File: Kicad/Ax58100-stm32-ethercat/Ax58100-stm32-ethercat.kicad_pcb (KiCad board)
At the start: 4 copper layers, 94.5 x 59.2 mm, 131 parts, among them J1 Conn_01x06_Pin, J10 Conn_01x02_Pin, J11 Stepper 2, J12 Serial usart1, J13 Stepper 1, J14 I2C bus2, J2 Encoder 1, J3 Conn_01x06_Pin, J4 Encoder 2, J5 Conn_01x06_Pin, J6 Encoder 4, J7 DAC1, J8 Encoder 3, J9 STLINK, SW1 SW PB, U1 AMS1117-1.2, U2 AX58100, U3 24LC32A, U4 STM32F407VGT6, U5 AMS1117-3.3, Y1 NXK25.000AE12F-KAB6-12, Y2 8 MHz

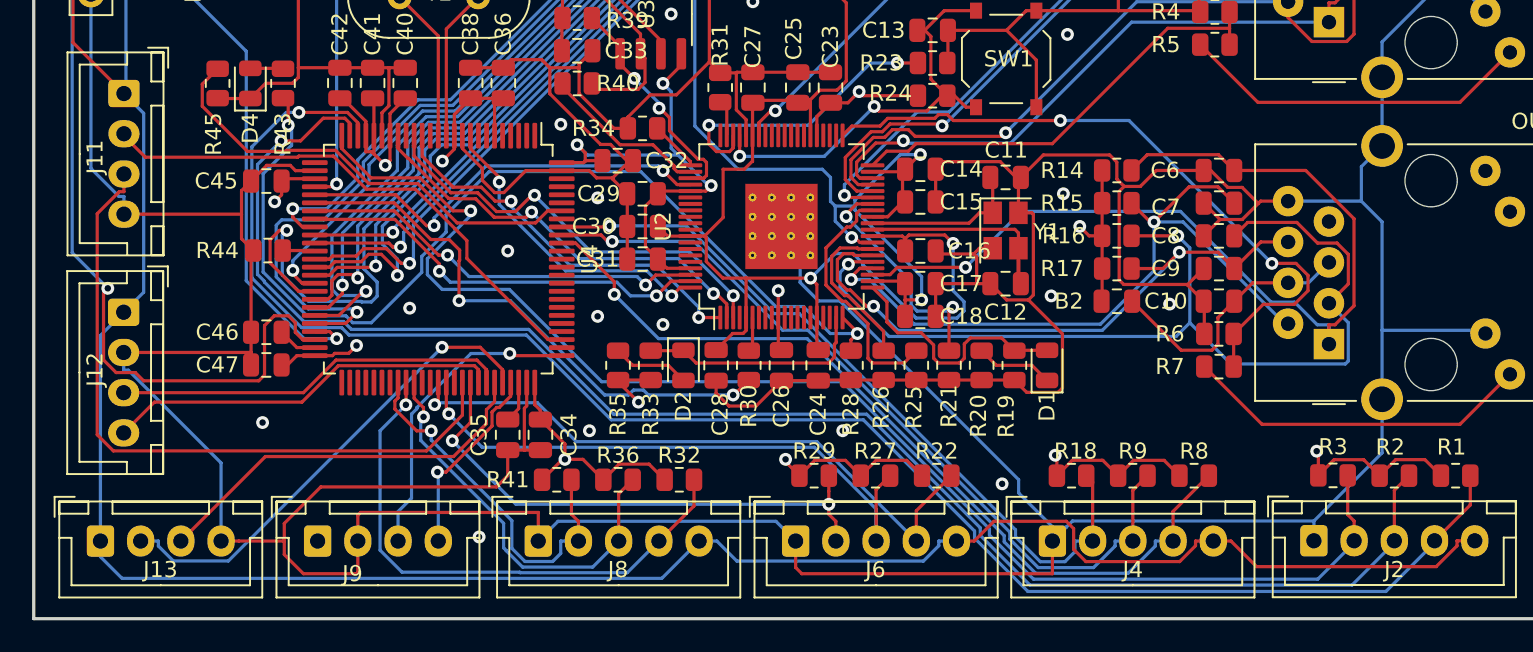
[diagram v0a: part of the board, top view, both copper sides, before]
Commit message: Added optional pull-down to step generators
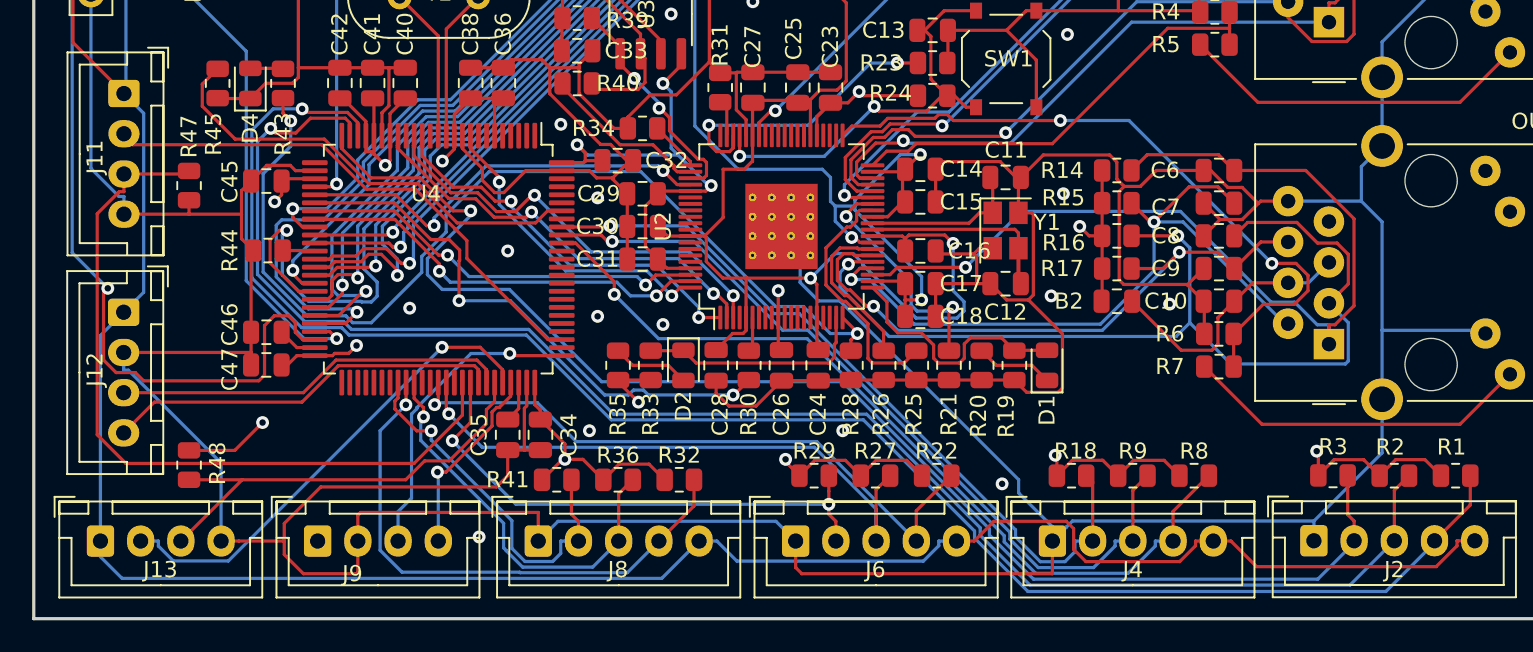
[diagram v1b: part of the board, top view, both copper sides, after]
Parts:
- added R47: NC, Resistor_SMD:R_0805_2012Metric, F.Cu at (148.6, 96.0)
- added R48: NC, Resistor_SMD:R_0805_2012Metric, F.Cu at (148.6, 113.4)
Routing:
- net GND: track 676.2 -> 682.4 mm
- net STEP2_STEP: track 43.1 -> 47.9 mm
- net STEP1_STEP: track 24.8 -> 28.1 mm
- net ENC1_B: track 99.3 -> 100.3 mm
- net ENC1_A: track 104.9 -> 105.7 mm

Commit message: First component placement
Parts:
- removed J14: I2C bus2, Connector_PinHeader_2.54mm:PinHeader_1x04_P2.54mm_Vertical
- removed J8: Encoder 3, Connector_JST:JST_XH_B5B-XH-A_1x05_P2.50mm_Vertical
- removed R22, R27, R3, R32, R36, R41, R8: 1k, Resistor_SMD:R_0805_2012Metric
- added D10: Yellow led, LED_SMD:LED_0603_1608Metric, F.Cu at (100.6, 34.3)
- added D11: Red led, LED_SMD:LED_0603_1608Metric, F.Cu at (100.5, 62.2)
- added D12: Yellow led, LED_SMD:LED_0603_1608Metric, F.Cu at (100.6, 29.1)
- added D13: Red led, LED_SMD:LED_0603_1608Metric, F.Cu at (100.5, 67.5)
- added D14: Red led, LED_SMD:LED_0603_1608Metric, F.Cu at (100.5, 30.8)
- added D15: Red led, LED_SMD:LED_0603_1608Metric, F.Cu at (100.5, 36.1)
- added D16: Red led, LED_SMD:LED_0603_1608Metric, F.Cu at (100.5, 41.3)
- added D17: Red led, LED_SMD:LED_0603_1608Metric, F.Cu at (100.5, 46.5)
- added D23: Yellow led, LED_SMD:LED_0603_1608Metric, F.Cu at (100.5, 50.0)
- added D25: Yellow led, LED_SMD:LED_0603_1608Metric, F.Cu at (100.6, 55.2)
- added D27: Yellow led, LED_SMD:LED_0603_1608Metric, F.Cu at (100.6, 60.5)
- added D29: Yellow led, LED_SMD:LED_0603_1608Metric, F.Cu at (100.6, 65.7)
- added D6: Yellow led, LED_SMD:LED_0603_1608Metric, F.Cu at (100.6, 44.8)
- added D7: Red led, LED_SMD:LED_0603_1608Metric, F.Cu at (100.6, 51.8)
- added D8: Yellow led, LED_SMD:LED_0603_1608Metric, F.Cu at (100.6, 39.5)
- added D9: Red led, LED_SMD:LED_0603_1608Metric, F.Cu at (100.5, 57.0)
- added J15: In1-4, TerminalBlock:TerminalBlock_bornier-4_P5.08mm, F.Cu at (107.0, 44.5)
- added J16: 24V Field, TerminalBlock:TerminalBlock_bornier-2_P5.08mm, F.Cu at (82.7, 45.2)
- added J17: In5-8, TerminalBlock:TerminalBlock_bornier-4_P5.08mm, F.Cu at (107.0, 66.0)
- added J19: Step3, TerminalBlock:TerminalBlock_bornier-3_P5.08mm, F.Cu at (122.9, 71.6)
- added J20: Step4, TerminalBlock:TerminalBlock_bornier-3_P5.08mm, F.Cu at (122.9, 87.4)
- added J21: THCAD, TerminalBlock:TerminalBlock_bornier-4_P5.08mm, F.Cu at (122.9, 108.5)
- added R49: 1k, Resistor_SMD:R_0603_1608Metric, F.Cu at (100.5, 43.0)
- added R50: 1k, Resistor_SMD:R_0603_1608Metric, F.Cu at (100.5, 37.8)
- added R51: 1k, Resistor_SMD:R_0603_1608Metric, F.Cu at (100.5, 32.6)
- added R52: 1k, Resistor_SMD:R_0603_1608Metric, F.Cu at (100.5, 27.3)
- added R53: 4.7k, Resistor_SMD:R_0805_2012Metric, F.Cu at (116.8, 50.5)
- added R57: 1k, Resistor_SMD:R_0603_1608Metric, F.Cu at (100.5, 48.3)
- added R58: 1k, Resistor_SMD:R_0603_1608Metric, F.Cu at (100.5, 53.5)
- added R59: 1k, Resistor_SMD:R_0603_1608Metric, F.Cu at (100.5, 58.7)
- added R60: 1k, Resistor_SMD:R_0603_1608Metric, F.Cu at (100.5, 64.0)
- added RN1: 40k, Resistor_SMD:R_Array_Convex_4x0603, F.Cu at (90.0, 39.5)
- added RN2: 40k, Resistor_SMD:R_Array_Convex_4x0603, F.Cu at (89.7, 57.8)
- added RN3: 1k, Resistor_SMD:R_Array_Convex_4x0603, F.Cu at (95.3, 57.8)
- added RN4: 1k, Resistor_SMD:R_Array_Convex_4x0603, F.Cu at (95.9, 39.5)
- added RN5: 330, Resistor_SMD:R_Array_Convex_4x0603, F.Cu at (95.1, 94.2)
- added U10: TXB0104PW, Package_SO:TSSOP-14_4.4x5mm_P0.65mm, F.Cu at (116.1, 74.6)
- added U11: MAX3485CSA/ESA, Package_SO:SO-8_3.9x4.9mm_P1.27mm, F.Cu at (115.6, 92.9)
- added U6: TLP292-4, Package_SO:SOIC-16_4.55x10.3mm_P1.27mm, F.Cu at (92.7, 32.0)
- added U7: TLP291-4, Package_SO:SOIC-16_4.55x10.3mm_P1.27mm, F.Cu at (97.1, 82.8)
- added U8: TLP292-4, Package_SO:SOIC-16_4.55x10.3mm_P1.27mm, F.Cu at (92.8, 50.4)
- added U9: TXB0104PW, Package_SO:TSSOP-14_4.4x5mm_P0.65mm, F.Cu at (115.8, 42.7)
- J1: value Conn_01x06_Pin -> Out_opt
- J10: value Conn_01x02_Pin -> 5V Power IN; footprint Connector_JST:JST_XH_B2B-XH-A_1x02_P2.50mm_Vertical -> TerminalBlock:TerminalBlock_bornier-2_P5.08mm
- J11: value Stepper 2 -> Step1; footprint Connector_JST:JST_XH_B4B-XH-A_1x04_P2.50mm_Vertical -> TerminalBlock:TerminalBlock_bornier-3_P5.08mm
- J13: value Stepper 1 -> Step2; footprint Connector_JST:JST_XH_B4B-XH-A_1x04_P2.50mm_Vertical -> TerminalBlock:TerminalBlock_bornier-3_P5.08mm
- J2: value Encoder 1 -> Output1-2; footprint Connector_JST:JST_XH_B5B-XH-A_1x05_P2.50mm_Vertical -> TerminalBlock:TerminalBlock_bornier-4_P5.08mm
- J3: value Conn_01x06_Pin -> In_opt1
- J4: value Encoder 2 -> Output3-4; footprint Connector_JST:JST_XH_B5B-XH-A_1x05_P2.50mm_Vertical -> TerminalBlock:TerminalBlock_bornier-4_P5.08mm
- J5: value Conn_01x06_Pin -> In_opt2
- J6: value Encoder 4 -> DAC; footprint Connector_JST:JST_XH_B5B-XH-A_1x05_P2.50mm_Vertical -> TerminalBlock:TerminalBlock_bornier-3_P5.08mm
- J7: value DAC1 -> Encoder; footprint Connector_JST:JST_XH_B3B-XH-A_1x03_P2.50mm_Vertical -> TerminalBlock:TerminalBlock_bornier-5_P5.08mm
- R18, R2: value 1k -> 4.7k
- R47: value NC -> 120
- R48: value NC -> 4.7k
- moved J1 195.8 mm to (38.1, 103.5), turned to 90 degrees
- moved OUT1 187.9 mm to (47.4, 30.2), turned to 90 degrees
- moved R7 176.7 mm to (54.3, 28.8), turned to 0 degrees
- moved IN1 175.7 mm to (47.4, 50.2), turned to 90 degrees
- moved R6 175.0 mm to (54.3, 30.8), turned to 0 degrees
- moved C10 173.3 mm to (54.3, 32.9), turned to 180 degrees
- moved C9 171.7 mm to (54.3, 34.9), turned to 180 degrees
- moved C8 170.1 mm to (54.3, 36.9), turned to 180 degrees
- moved D1 169.5 mm to (37.0, 67.9), turned to -90 degrees
- moved C7 168.7 mm to (54.3, 39.0), turned to 180 degrees
- moved C6 167.3 mm to (54.3, 41.0), turned to 180 degrees
- moved J3 166.2 mm to (51.4, 110.5)
- moved R19 165.6 mm to (39.0, 67.9), turned to -90 degrees
- moved R5 162.5 mm to (54.5, 48.8), turned to 0 degrees
- moved C12 162.4 mm to (39.6, 73.0), turned to 0 degrees
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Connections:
- J11 pad 1: +5V -> STEP1_DIR_OUT
- J11 pad 2: STEP2_DIR -> STEP1_STEP_OUT
- J11 pad 3: STEP2_STEP -> GND
- J13 pad 1: +5V -> STEP2_DIR_OUT
- J13 pad 2: STEP1_DIR -> STEP2_STEP_OUT
- J13 pad 3: STEP1_STEP -> GND
- J2 pad 1: GND -> Net-(J2-Pin_1)
- J2 pad 2: ENC1_Z -> Net-(J2-Pin_2)
- J2 pad 3: ENC1_B -> Net-(J2-Pin_3)
- J2 pad 4: ENC1_A -> Net-(J2-Pin_4)
- J4 pad 1: GND -> Net-(J4-Pin_1)
- J4 pad 2: ENC2_Z -> Net-(J4-Pin_2)
- J4 pad 3: ENC2_B -> Net-(J4-Pin_3)
- J4 pad 4: ENC2_A -> Net-(J4-Pin_4)
- J6 pad 1: GND -> +3.3V
- J6 pad 2: ENC4_Z -> DAC1
- J6 pad 3: ENC4_B -> GND
- J7 pad 1: +3.3V -> +5V
- J7 pad 2: DAC1 -> ENC_A
- J7 pad 3: GND -> ENC_B
- R1 pad 1: ENC1_A -> ENC_A
- R1 pad 2: +3.3V -> +5V
- R18 pad 1: ENC2_Z -> GND
- R18 pad 2: +3.3V -> STEP4_STEP
- R2 pad 1: ENC1_B -> GND
- R2 pad 2: +3.3V -> STEP3_STEP
- R29 pad 1: ENC4_Z -> ENC_Z
- R29 pad 2: +3.3V -> +5V
- R47 pad 1: STEP2_STEP -> Net-(J21-Pin_2)
- R47 pad 2: GND -> Net-(J21-Pin_3)
- R48 pad 1: STEP1_STEP -> GND
- R48 pad 2: GND -> STEP1_STEP
- R9 pad 1: ENC2_B -> ENC_B
- R9 pad 2: +3.3V -> +5V
- U4 pad 23: ENC1_A -> ENC_A
- U4 pad 24: ENC1_B -> ENC_B
- U4 pad 25: ENC1_Z -> THCAD_CTR
- U4 pad 26: unconnected-(U4-PA3-Pad26) -> ENC_Z
- U4 pad 3: unconnected-(U4-PE4-Pad3) -> STEP4_DIR
- U4 pad 4: unconnected-(U4-PE5-Pad4) -> STEP4_STEP
- U4 pad 47: I2C2_SCL -> unconnected-(U4-PB10-Pad47)
- U4 pad 48: I2C2_SDA -> unconnected-(U4-PB11-Pad48)
- U4 pad 58: ENC3_Z -> STEP3_DIR
- U4 pad 59: ENC3_A -> STEP3_STEP
- U4 pad 60: ENC3_B -> unconnected-(U4-PD13-Pad60)
- U4 pad 63: ENC4_A -> unconnected-(U4-PC6-Pad63)
- U4 pad 64: ENC4_B -> unconnected-(U4-PC7-Pad64)
- U4 pad 65: unconnected-(U4-PC8-Pad65) -> STEP2_DIR
- U4 pad 67: ENC4_Z -> unconnected-(U4-PA8-Pad67)
- U4 pad 78: STEP2_DIR -> unconnected-(U4-PC10-Pad78)
- U4 pad 90: ENC2_A -> unconnected-(U4-PB4-Pad90)
- U4 pad 91: ENC2_B -> unconnected-(U4-PB5-Pad91)
- U4 pad 92: ENC2_Z -> unconnected-(U4-PB6-Pad92)
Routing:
- net GND: track 682.4 -> 0.00 mm, vias 24 -> 0
- net +5V: track 289.8 -> 0.00 mm, vias 1 -> 0
- net +3.3V: track 209.3 -> 0.00 mm, vias 23 -> 0
- net +3.3VA: track 109.3 -> 0.00 mm, vias 4 -> 0
- net ENC1_A: track 105.7 -> 0.00 mm, vias 1 -> 0
- net ENC1_B: track 100.3 -> 0.00 mm, vias 1 -> 0
- net +1V2: track 97.9 -> 0.00 mm, vias 2 -> 0
- net IO1: track 93.0 -> 0.00 mm, vias 1 -> 0
- net ENC1_Z: track 86.5 -> 0.00 mm, vias 1 -> 0
- net IO2: track 83.8 -> 0.00 mm, vias 1 -> 0
- net IO3: track 81.9 -> 0.00 mm, vias 1 -> 0
- net IO4: track 80.7 -> 0.00 mm, vias 1 -> 0
- net IO8: track 77.5 -> 0.00 mm, vias 1 -> 0
- net P0_TXON: track 75.4 -> 0.00 mm, vias 1 -> 0
- net IO5: track 72.0 -> 0.00 mm, vias 1 -> 0
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- removed copper zone on In2.Cu, net +3.3V
- removed copper zone on B.Cu, net GND
- removed copper zone on F.Cu, net GND
- removed copper zone on In1.Cu, net GND
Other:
- board size 94.5 x 59.2 mm -> 95.3 x 89.4 mm

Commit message: Two-layer now
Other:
- copper layers 4 -> 2
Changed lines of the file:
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@@
   (layers
     (0 "F.Cu" signal)
-    (1 "In1.Cu" power "GND.Cu")
-    (2 "In2.Cu" power "Power.Cu")
     (31 "B.Cu" signal)
     (32 "B.Adhes" user "B.Adhesive")
@@
       (layer "F.Mask" (type "Top Solder Mask") (thickness 0.01))
       (layer "F.Cu" (type "copper") (thickness 0.035))
-      (layer "dielectric 1" (type "prepreg") (thickness 0.1) (material "FR4") (epsilon_r 4.5) (loss_tangent 0.02))
-      (layer "In1.Cu" (type "copper") (thickness 0.035))
-      (layer "dielectric 2" (type "core") (thickness 1.24) (material "FR4") (epsilon_r 4.5) (loss_tangent 0.02))
-      (layer "In2.Cu" (type "copper") (thickness 0.035))
-      (layer "dielectric 3" (type "prepreg") (thickness 0.1) (material "FR4") (epsilon_r 4.5) (loss_tangent 0.02))
+      (layer "dielectric 1" (type "core") (thickness 1.51) (material "FR4") (epsilon_r 4.5) (loss_tangent 0.02))
       (layer "B.Cu" (type "copper") (thickness 0.035))
       (layer "B.Mask" (type "Bottom Solder Mask") (thickness 0.01))

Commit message: wip
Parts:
- removed the U10 at (116.1, 74.6)
- removed the U9 at (115.8, 42.7)
- added C50: 0.1uF, Capacitor_SMD:C_0805_2012Metric, F.Cu at (167.5, 75.9)
- added C51: 0.1uF, Capacitor_SMD:C_0805_2012Metric, F.Cu at (167.5, 78.0)
- added C52: 0.1uF, Capacitor_SMD:C_0805_2012Metric, F.Cu at (169.2, 112.3)
- added U12: TXS0108EPW, Package_SO:TSSOP-20_4.4x6.5mm_P0.65mm, F.Cu at (167.4, 82.5)
- U4: renamed from U7; value TLP291-4 -> TLP292-4
- moved R14 88.8 mm to (141.6, 123.7), turned to -90 degrees
- moved C2 85.3 mm to (139.5, 123.7), turned to -90 degrees
- moved C4 82.1 mm to (137.4, 123.7), turned to 90 degrees
- moved C1 72.2 mm to (141.0, 102.1), turned to 90 degrees
- moved SW1 64.4 mm to (97.3, 109.4)
- moved C3 64.4 mm to (137.2, 101.8), turned to 90 degrees
- moved U7 62.9 mm to (133.1, 112.7), turned to -90 degrees
- moved RN1 61.4 mm to (149.5, 122.7)
- moved C5 61.3 mm to (135.2, 92.1), turned to 0 degrees
- moved U4 61.2 mm to (149.4, 114.8)
- moved C6 60.3 mm to (135.1, 101.8), turned to 90 degrees
- moved C42 60.3 mm to (96.9, 117.8)
- moved R47 60.3 mm to (96.9, 115.8)
- moved R46 60.3 mm to (96.9, 113.8)
- moved R1 59.9 mm to (151.6, 96.8)
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- renumbered B7 to B1, B6 to B2, B5 to B3, B2 to B4, B1 to B5, B4 to B6, B3 to B7, C32 to C1, C42 to C10, C49 to C11, C48 to C12, C45 to C13, C46 to C14, C47 to C15, C44 to C16, C43 to C17, C33 to C18, C31 to C19, C34 to C2, C30 to C20, C29 to C21, C28 to C22, C27 to C23, C10 to C24, C9 to C25, C8 to C26, C7 to C27, C6 to C28, C5 to C29, C36 to C3, C4 to C30, C3 to C31, C2 to C32, C1 to C33, C26 to C34, C25 to C35, C24 to C36, C23 to C37, C22 to C38, C21 to C39, C35 to C4, C20 to C40, C19 to C41, C13 to C42, C18 to C43, C17 to C44, C16 to C45, C15 to C46, C14 to C47, C12 to C48, C11 to C49, C37 to C5, C38 to C6, C39 to C7, C40 to C8, C41 to C9, D12 to D1, D7 to D10, D25 to D11, D9 to D12, D27 to D13, D11 to D14, D29 to D15, D13 to D16, D5 to D17, D4 to D18, D3 to D19, D14 to D2, D2 to D20, D1 to D21, D10 to D3, D15 to D4, D8 to D5, D16 to D6, D6 to D7, D17 to D8, D23 to D9, J11 to J1, J16 to J11, J6 to J12, J7 to J13, J5 to J14, J9 to J15, J12 to J16, J3 to J17, J1 to J18, J13 to J2, J19 to J3, J20 to J4, J21 to J5, J15 to J6, J17 to J7, J2 to J8, J4 to J9, R48 to R1, R57 to R10, R58 to R11, R59 to R12, R60 to R13, R35 to R14, R29 to R15, R9 to R16, R1 to R17, R46 to R18, R45 to R19, R53 to R2, R43 to R20, R44 to R21, R42 to R22, R40 to R23, R39 to R24, R38 to R25, R37 to R26, R33 to R27, R34 to R28, R17 to R29, R2 to R3, R16 to R30, R15 to R31, R14 to R32, R13 to R33, R12 to R34, R11 to R35, R10 to R36, R31 to R37, R30 to R38, R7 to R39, R18 to R4, R6 to R40, R5 to R41, R4 to R42, R28 to R43, R26 to R44, R25 to R45, R24 to R46, R23 to R47, R21 to R48, R20 to R49, R47 to R5, R19 to R50, R52 to R6, R51 to R7, R50 to R8, R49 to R9, RN5 to RN1, RN4 to RN2, RN1 to RN4, RN2 to RN5, U1 to U10, U2 to U11, U11 to U3, U6 to U5, U8 to U6, U4 to U7, U5 to U8, U3 to U9, Y2 to Y1, Y1 to Y2
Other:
- board size 95.3 x 89.4 mm -> 95.3 x 87.9 mm

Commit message: resistor overhaul
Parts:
- removed RN1: 330, Resistor_SMD:R_Array_Convex_4x0603
- removed RN2, RN3: 1k, Resistor_SMD:R_Array_Convex_4x0603
- removed RN4, RN5: 40k, Resistor_SMD:R_Array_Convex_4x0603
- added R51: 1k, Resistor_SMD:R_0603_1608Metric, F.Cu at (147.6, 81.0)
- added R52: 1k, Resistor_SMD:R_0603_1608Metric, F.Cu at (147.6, 82.5)
- added R53: 1k, Resistor_SMD:R_0603_1608Metric, F.Cu at (147.6, 84.1)
- added R54: 1k, Resistor_SMD:R_0603_1608Metric, F.Cu at (147.6, 85.6)
- added R55: 1k, Resistor_SMD:R_0603_1608Metric, F.Cu at (147.3, 62.5)
- added R56: 1k, Resistor_SMD:R_0603_1608Metric, F.Cu at (147.3, 64.0)
- added R57: 1k, Resistor_SMD:R_0603_1608Metric, F.Cu at (147.3, 65.5)
- added R58: 1k, Resistor_SMD:R_0603_1608Metric, F.Cu at (147.3, 67.1)
- added R59: 330, Resistor_SMD:R_0603_1608Metric, F.Cu at (147.1, 107.4)
- added R60: 330, Resistor_SMD:R_0603_1608Metric, F.Cu at (148.6, 107.4)
- added R61: 330, Resistor_SMD:R_0603_1608Metric, F.Cu at (150.1, 107.4)
- added R62: 330, Resistor_SMD:R_0603_1608Metric, F.Cu at (151.6, 107.4)
- added R63: 39k, Resistor_SMD:R_0603_1608Metric, F.Cu at (143.0, 62.5)
- added R64: 39k, Resistor_SMD:R_0603_1608Metric, F.Cu at (143.0, 64.0)
- added R65: 39k, Resistor_SMD:R_0603_1608Metric, F.Cu at (143.0, 65.5)
- added R66: 39k, Resistor_SMD:R_0603_1608Metric, F.Cu at (143.0, 67.1)
- added R67: 39k, Resistor_SMD:R_0603_1608Metric, F.Cu at (142.7, 81.0)
- added R68: 39k, Resistor_SMD:R_0603_1608Metric, F.Cu at (142.7, 82.5)
- added R69: 39k, Resistor_SMD:R_0603_1608Metric, F.Cu at (142.7, 84.1)
- added R70: 39k, Resistor_SMD:R_0603_1608Metric, F.Cu at (142.7, 85.6)

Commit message: Might be in final shape.
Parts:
- J1, J2, J3, J4: footprint TerminalBlock:TerminalBlock_bornier-3_P5.08mm -> Connector_Phoenix_MC:PhoenixContact_MCV_1,5_3-G-3.5_1x03_P3.50mm_Vertical
- J10: renamed from J13; footprint TerminalBlock:TerminalBlock_bornier-5_P5.08mm -> Connector_Phoenix_MC:PhoenixContact_MCV_1,5_5-G-3.5_1x05_P3.50mm_Vertical
- J11: renamed from J10; footprint TerminalBlock:TerminalBlock_bornier-2_P5.08mm -> Connector_Phoenix_MC:PhoenixContact_MCV_1,5_2-G-3.5_1x02_P3.50mm_Vertical
- J12: renamed from J11; footprint TerminalBlock:TerminalBlock_bornier-2_P5.08mm -> Connector_Phoenix_MC:PhoenixContact_MCV_1,5_2-G-3.5_1x02_P3.50mm_Vertical
- J13: renamed from J12; footprint TerminalBlock:TerminalBlock_bornier-3_P5.08mm -> Connector_Phoenix_MC:PhoenixContact_MCV_1,5_3-G-3.5_1x03_P3.50mm_Vertical
- J5, J6, J7, J8, J9: footprint TerminalBlock:TerminalBlock_bornier-4_P5.08mm -> Connector_Phoenix_MC:PhoenixContact_MCV_1,5_4-G-3.5_1x04_P3.50mm_Vertical
- R10: renamed from R1; value 4.7k -> 4k7
- R13: renamed from R2; value 4.7k -> 4k7
- R17: renamed from R3; value 4.7k -> 4k7
- R2: renamed from R6; value 1k -> 4k7
- R28: renamed from R4; value 4.7k -> 4k7
- R3: renamed from R7; value 1k -> 4k7
- R4: renamed from R8; value 1k -> 4k7
- R5: renamed from R9; value 1k -> 4k7
- R6: renamed from R10; value 1k -> 4k7
- R7: renamed from R11; value 1k -> 4k7
- R8: renamed from R12; value 1k -> 4k7
- R9: renamed from R13; value 1k -> 4k7
- moved J14 51.3 mm to (125.5, 86.2), turned to 90 degrees
- moved J16 46.2 mm to (118.6, 86.2), turned to 90 degrees
- moved R56 44.0 mm to (112.0, 91.2), turned to 90 degrees
- moved C13 32.2 mm to (129.0, 55.1)
- moved C15 32.2 mm to (127.0, 55.1)
- moved J9 29.6 mm to (158.4, 103.5), turned to -90 degrees
- moved J5 26.3 mm to (174.9, 106.0), turned to -90 degrees
- moved R12 26.1 mm to (152.1, 112.9)
- moved J8 24.8 mm to (158.4, 87.0), turned to -90 degrees
- moved D18 22.7 mm to (125.7, 68.6)
- moved R38 22.7 mm to (129.8, 68.6)
- moved D17 22.7 mm to (127.8, 68.6)
- moved R39 22.7 mm to (123.7, 68.6)
- moved R15 22.7 mm to (150.1, 112.9)
- moved R62 21.1 mm to (104.6, 91.2), turned to 90 degrees
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- renumbered B4 to B2, B5 to B3, B2 to B4, B3 to B5, C52 to C1, C7 to C10, C8 to C11, C9 to C12, C12 to C13, C10 to C14, C17 to C15, C22 to C16, C13 to C17, C14 to C18, C15 to C19, C50 to C2, C34 to C20, C36 to C21, C18 to C22, C19 to C23, C20 to C24, C21 to C25, C11 to C26, C23 to C27, C24 to C28, C25 to C29, C51 to C3, C26 to C30, C27 to C31, C28 to C32, C29 to C33, C30 to C34, C31 to C35, C32 to C36, C33 to C37, C16 to C38, C35 to C39, C2 to C4, C37 to C40, C38 to C41, C39 to C42, C40 to C43, C41 to C44, C42 to C45, C43 to C46, C44 to C47, C45 to C48, C46 to C49, C4 to C5, C47 to C50, C48 to C51, C49 to C52, C1 to C6, C3 to C7, C5 to C8, C6 to C9, D19 to D18, D20 to D19, D18 to D20, J17 to J14, J16 to J15, J14 to J16, J15 to J17, R5 to R1, R62 to R11, R17 to R12, R61 to R14, R16 to R15, R60 to R16, R15 to R18, R55 to R19, R56 to R20, R57 to R21, R58 to R22, R51 to R23, R52 to R24, R53 to R25, R54 to R26, R59 to R27, R19 to R29, R63 to R30, R64 to R31, R65 to R32, R66 to R33, R67 to R34, R68 to R35, R69 to R36, R70 to R37, R18 to R38, R22 to R39, R21 to R40, R26 to R41, R38 to R42, R25 to R43, R24 to R44, R28 to R45, R23 to R46, R27 to R47, R29 to R48, R30 to R49, R31 to R50, R32 to R51, R33 to R52, R34 to R53, R35 to R54, R36 to R55, R14 to R56, R37 to R57, R39 to R58, R40 to R59, R41 to R60, R42 to R61, R20 to R62, R43 to R63, R44 to R64, R45 to R65, R46 to R66, R47 to R67, R48 to R68, R49 to R69, R50 to R70, U3 to U1, U11 to U10, U12 to U2, U4 to U3, U5 to U4, U6 to U5, U7 to U6, U8 to U7, U9 to U8, U10 to U9
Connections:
- J6 pad 1: Net-(D7-A) -> Net-(D1-A)
- J6 pad 2: Net-(D5-A) -> Net-(D3-A)
- J6 pad 3: Net-(D3-A) -> Net-(D5-A)
- J6 pad 4: Net-(D1-A) -> Net-(D7-A)
- J7 pad 1: Net-(D15-A) -> Net-(D10-K)
- J7 pad 2: Net-(D13-A) -> Net-(D11-A)
- J7 pad 3: Net-(D11-A) -> Net-(D13-A)
- J7 pad 4: Net-(D10-K) -> Net-(D15-A)
- R1 pad 1: Net-(J5-Pin_2) -> Net-(J5-Pin_3)
- R1 pad 2: Net-(J5-Pin_3) -> Net-(J5-Pin_2)
- U1 pad 6: Net-(J5-Pin_2) -> Net-(J5-Pin_3)
- U1 pad 7: Net-(J5-Pin_3) -> Net-(J5-Pin_2)
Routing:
- net GND: track 0.00 -> 841.0 mm, vias 0 -> 117
- net +3.3V: track 0.00 -> 463.8 mm, vias 0 -> 5
- net +5V: track 0.00 -> 247.1 mm, vias 0 -> 1
- net IO4: track 0.00 -> 119.2 mm, vias 0 -> 2
- net +1V2: track 0.00 -> 107.8 mm, vias 0 -> 3
- net IO12: track 0.00 -> 102.6 mm, vias 0 -> 1
- net IO10: track 0.00 -> 87.8 mm, vias 0 -> 1
- net +3.3VA: track 0.00 -> 85.2 mm
- net IO11: track 0.00 -> 85.0 mm, vias 0 -> 2
- net P1_TXOP: track 0.00 -> 81.7 mm, vias 0 -> 1
- net SWDIO: track 0.00 -> 78.1 mm, vias 0 -> 1
- net IO8: track 0.00 -> 77.8 mm, vias 0 -> 1
- net IO1: track 0.00 -> 75.6 mm, vias 0 -> 3
- net SWCLK: track 0.00 -> 75.6 mm, vias 0 -> 1
- net IO7: track 0.00 -> 73.7 mm, vias 0 -> 3
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- added copper zone on B.Cu, net GND
- added copper zone on F.Cu, net GND
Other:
- board size 95.3 x 87.9 mm -> 94.5 x 74.4 mm
